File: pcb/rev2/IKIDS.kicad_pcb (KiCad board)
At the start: 2 copper layers, 152.4 x 95.2 mm, 40 parts, among them SW1 SW_Push, U1 ATmega32U4-AU, Y1 16MHz

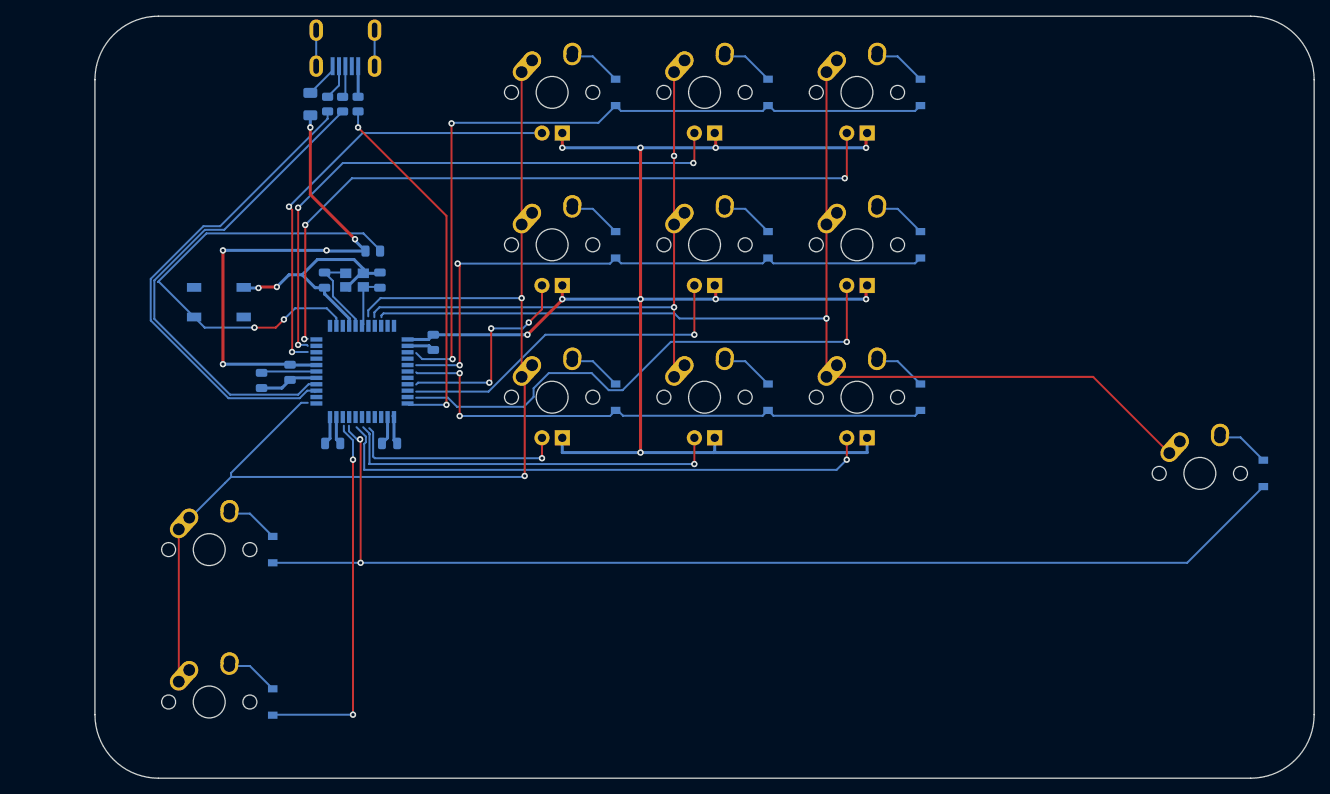
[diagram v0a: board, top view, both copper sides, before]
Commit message: added PCB files that doesn't require elite-c
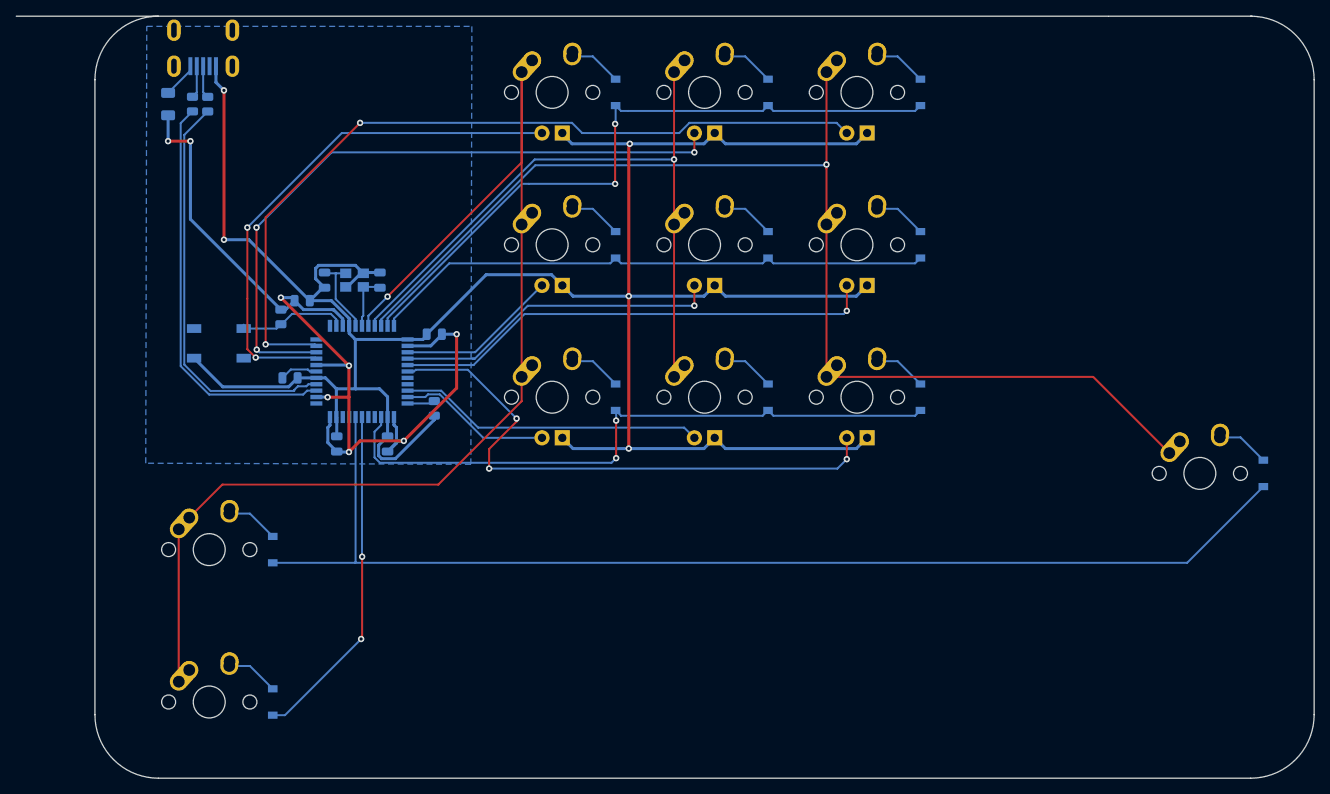
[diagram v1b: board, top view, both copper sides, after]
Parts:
- moved R4 39.2 mm to (74.2, 112.5), turned to 90 degrees
- moved F1 17.8 mm to (40.9, 74.5)
- moved USB1 17.8 mm to (45.3, 65.2)
- moved R1 16.9 mm to (43.9, 74.5)
- moved R3 16.9 mm to (45.8, 74.5)
- moved R2 14.1 mm to (55.0, 101.1), turned to 270 degrees
- moved C3 9.08 mm to (57.7, 99.1), turned to 0 degrees
- moved SW1 5.14 mm to (47.2, 104.4), turned to 180 degrees
- moved C7 3.57 mm to (56.1, 108.7), turned to 0 degrees
- moved C2 1.03 mm to (74.2, 103.3), turned to 180 degrees
- moved C4 0.51 mm to (62.0, 117.0), turned to 90 degrees
- moved C1 0.26 mm to (68.3, 117.0), turned to 90 degrees
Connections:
- U1 pad 10: Net-(U1-Pad10) -> led2
- U1 pad 18: Net-(U1-Pad18) -> col0
- U1 pad 19: Net-(U1-Pad19) -> col1
- U1 pad 20: Net-(U1-Pad20) -> col2
- U1 pad 21: Net-(U1-Pad21) -> row0
- U1 pad 22: Net-(U1-Pad22) -> row1
- U1 pad 25: Net-(U1-Pad25) -> led3
- U1 pad 26: Net-(U1-Pad26) -> led4
- U1 pad 27: Net-(U1-Pad27) -> led5
- U1 pad 28: Net-(U1-Pad28) -> led8
- U1 pad 31: Net-(U1-Pad31) -> led7
- U1 pad 32: Net-(U1-Pad32) -> led6
- U1 pad 36: Net-(U1-Pad36) -> row2
- U1 pad 39: Net-(U1-Pad39) -> row4
- U1 pad 40: Net-(U1-Pad40) -> row3
- U1 pad 8: Net-(U1-Pad8) -> led0
- U1 pad 9: Net-(U1-Pad9) -> led1
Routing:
- net GND: track 241.1 -> 307.5 mm, vias 12 -> 6
- net +5V: track 74.2 -> 118.9 mm, vias 5 -> 8
- net Net-(R2-Pad2): track 58.4 -> 13.9 mm, vias 2 -> 0
- net Net-(R4-Pad2): track 46.2 -> 3.46 mm, vias 2 -> 0
- net led2: track 90.4 -> 101.5 mm, vias 3 -> 2
- net row2: track 70.4 -> 81.3 mm
- net Net-(R1-Pad1): track 61.9 -> 51.1 mm
- net Net-(R3-Pad1): track 61.8 -> 51.2 mm
- net led7: track 48.9 -> 38.3 mm, vias 1 -> 0
- net led0: track 55.7 -> 66.1 mm
- net led1: track 73.9 -> 83.9 mm
- net row0: track 95.0 -> 85.4 mm
- net Net-(USB1-Pad6): track 9.00 -> 0.00 mm
- net col2: track 141.1 -> 149.7 mm
- net led6: track 27.5 -> 19.2 mm, vias 1 -> 0
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- added copper zone on B.Cu, net GND
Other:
- board size 152.4 x 95.2 mm -> 162.2 x 95.2 mm
